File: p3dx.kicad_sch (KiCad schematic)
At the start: 57 parts, among them J10 Switched Radio, J12 IR2, J18 IR3, J19 Unlabeled, J28 H8 MICRO-CONTROLLER, J30 Charger, J31 +12V_BAT, J32 GND_BAT, J37 Cooling Fan, J38 Unlabeled, J8 IR0, J9 IR1, Q10 NPN, Q12 NPN, Q13 NPN, Q17 IRF5305, Q18 IRF5305, Q19 IRF5305, Q20 IRF5305, Q9 NPN, U10 TS922I, U11 LM35DT, U3 74HC14, U7 PT78ST105V, U8 74HC14, U9 TS922I

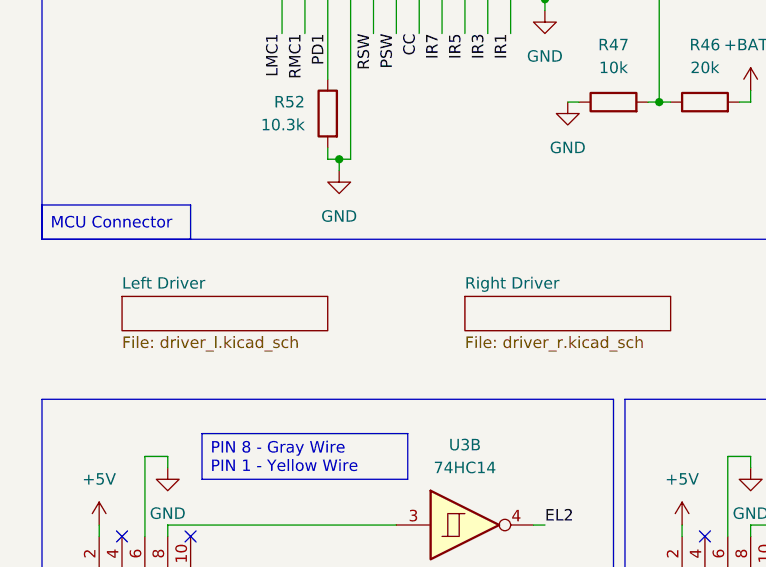
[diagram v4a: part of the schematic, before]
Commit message: Upgrad left driver scheme
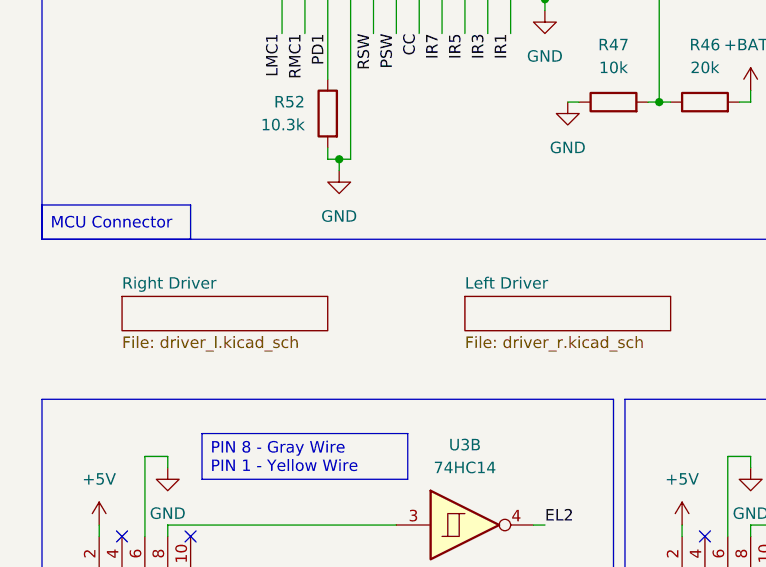
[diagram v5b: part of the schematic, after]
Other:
- sheet Left Driver: file driver_l.kicad_sch -> driver_r.kicad_sch
- sheet Right Driver: file driver_r.kicad_sch -> driver_l.kicad_sch
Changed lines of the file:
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@@
 			(color 0 0 0 0.0000)
 		)
-		(property "Sheetname" "Right Driver"
+		(property "Sheetname" "Left Driver"
 			(at 59.69 78.0284 0)
 			(effects
@@
 			(color 0 0 0 0.0000)
 		)
-		(property "Sheetname" "Left Driver"
+		(property "Sheetname" "Right Driver"
 			(at 21.59 78.0284 0)
 			(effects

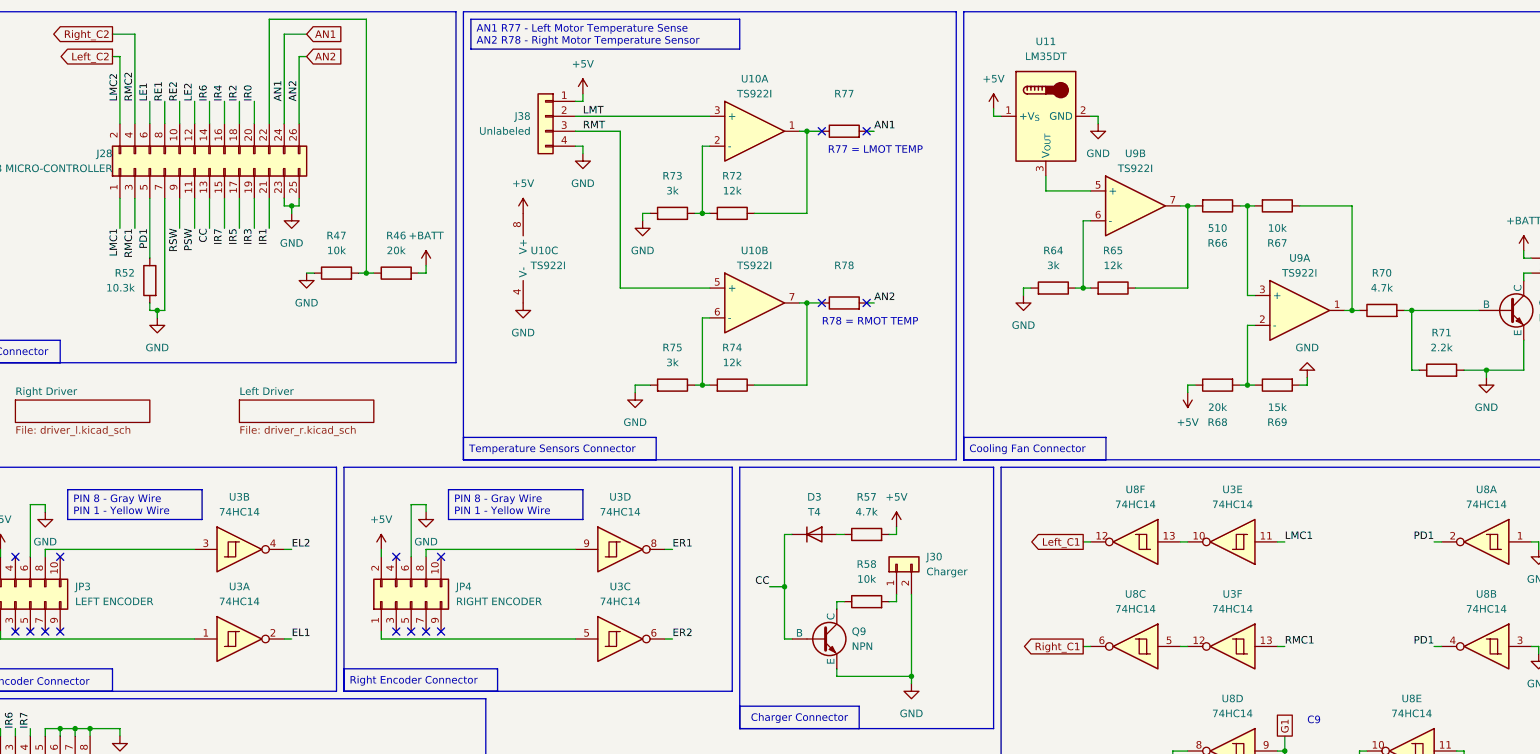
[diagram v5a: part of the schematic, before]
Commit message: Update J28 pin name
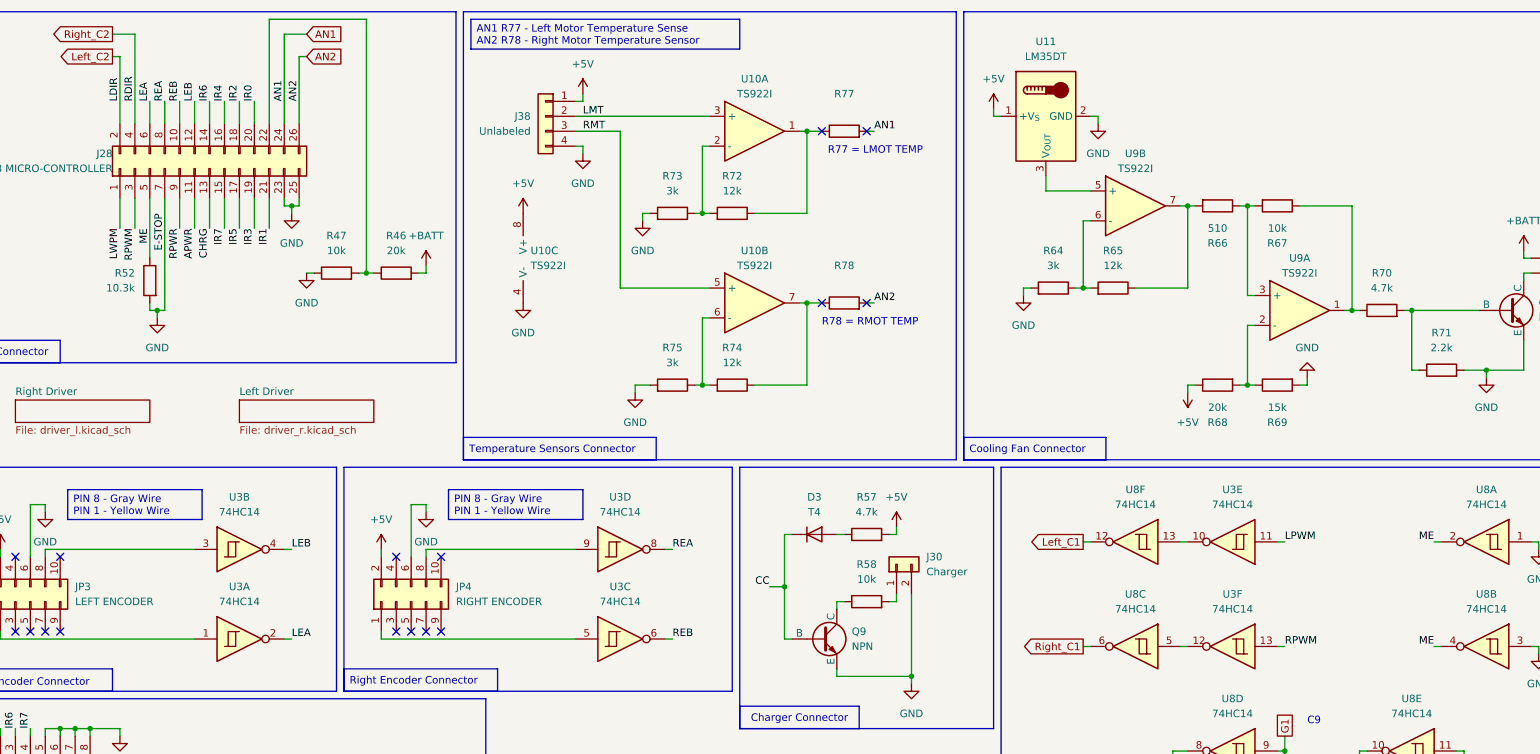
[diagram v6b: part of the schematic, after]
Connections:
- net LE1 is gone; now on net LEA: J28.6 (Pin_6)
- net LE2 is gone; now on net LEB: J28.12 (Pin_12)
- net RE1 is gone; now on net REA: J28.8 (Pin_8)
- net RE2 is gone; now on net REB: J28.10 (Pin_10)
- net CC: no longer J28.13 (Pin_13)
- net PSW: no longer J28.11 (Pin_11)
- net RSW: no longer J28.9 (Pin_9)
- net EL1 renamed LEA
- net EL2 renamed LEB
- net ER1 renamed REA
- net ER2 renamed REB
- net LMC1 renamed LPWM
- net LPWM: no longer J28.1 (Pin_1)
- net PD1 renamed ME
- net RMC1 renamed RPWM
- new net APWR: J28.11 (Pin_11)
- new net CHRG: J28.13 (Pin_13)
- new net LWPM: J28.1 (Pin_1)
- new net RPWR: J28.9 (Pin_9)
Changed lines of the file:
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@@
 		)
 	)
-	(label "LMC1"
+	(label "LPWM"
 		(at 237.49 102.87 0)
 		(effects
@@
 		)
 	)
-	(label "EL1"
+	(label "LEA"
 		(at 68.58 119.38 0)
 		(effects
@@
 		)
 	)
-	(label "LE2"
+	(label "LEB"
 		(at 52.07 27.94 90)
 		(effects
@@
 		)
 	)
-	(label "PD1"
+	(label "ME"
 		(at 262.89 102.87 180)
 		(effects
@@
 		)
 	)
-	(label "RMC1"
+	(label "RPWM"
 		(at 237.49 120.65 0)
 		(effects
@@
 		)
 	)
-	(label "RE2"
+	(label "REB"
 		(at 49.53 27.94 90)
 		(effects
@@
 		)
 	)
-	(label "RMC2"
+	(label "RDIR"
 		(at 41.91 27.94 90)
 		(effects
@@
 		)
 	)
-	(label "CC"
+	(label "CHRG"
 		(at 54.61 49.53 270)
 		(effects
@@
 		)
 	)
-	(label "PD1"
+	(label "ME"
 		(at 262.89 120.65 180)
 		(effects
@@
 		)
 	)
-	(label "RMC1"
+	(label "RPWM"
 		(at 41.91 49.53 270)
 		(effects
@@
 		)
 	)
-	(label "LMC2"
+	(label "LDIR"
 		(at 39.37 27.94 90)
 		(effects
@@
 		)
 	)
-	(label "RE1"
+	(label "REA"
 		(at 46.99 27.94 90)
 		(effects
@@
 		)
 	)
+	(label "E-STOP"
+		(at 46.99 46.99 270)
+		(effects
+			(font
+				(size 1.27 1.27)
+			)
+			(justify right bottom)
+		)
+	)
 	(label "IR2"
 		(at 80.01 147.32 270)
@@
 		)
 	)
-	(label "RSW"
+	(label "RPWR"
 		(at 49.53 49.53 270)
 		(effects
@@
 		)
 	)
-	(label "LMC1"
+	(label "LWPM"
 		(at 39.37 49.53 270)
 		(effects
@@
 		)
 	)
-	(label "PSW"
+	(label "APWR"
 		(at 52.07 49.53 270)
 		(effects
@@
 		)
 	)
-	(label "ER1"
+	(label "REA"
 		(at 133.35 104.14 0)
 		(effects
@@
 		)
 	)
-	(label "PD1"
+	(label "ME"
 		(at 44.45 49.53 270)
 		(effects
@@
 		)
 	)
-	(label "LE1"
+	(label "LEA"
 		(at 44.45 27.94 90)
 		(effects
@@
 		)
 	)
-	(label "ER2"
+	(label "REB"
 		(at 133.35 119.38 0)
 		(effects
@@
 		)
 	)
-	(label "EL2"
+	(label "LEB"
 		(at 68.58 104.14 0)
 		(effects

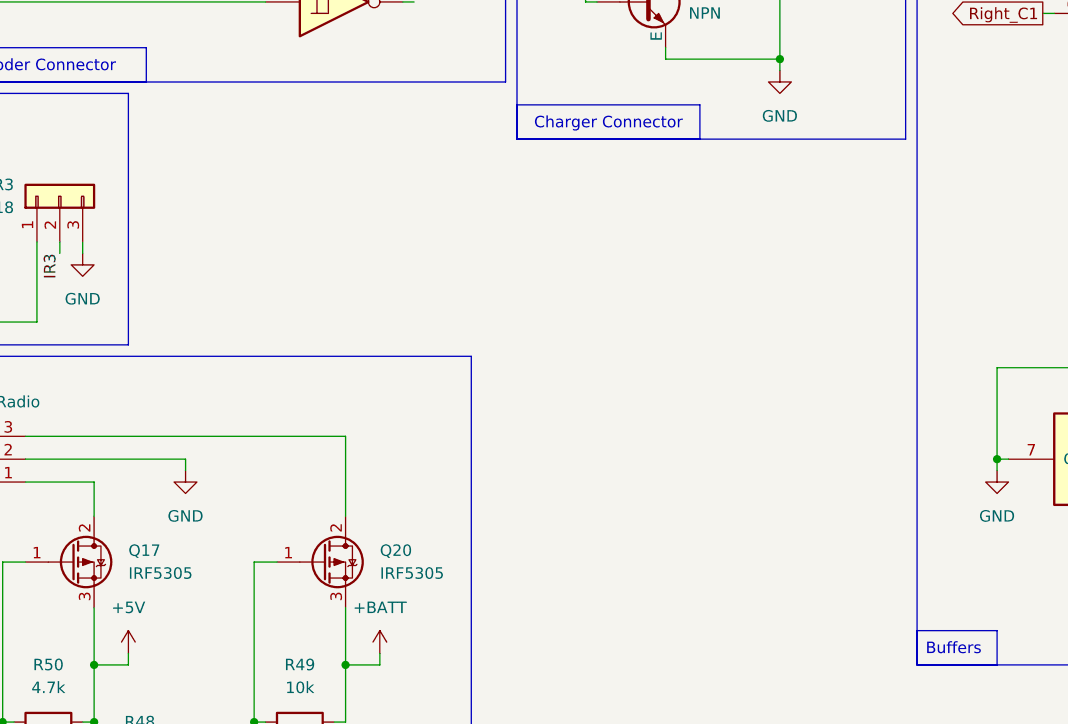
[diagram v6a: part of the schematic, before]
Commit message: Update driver scheme and added User Control Panel scheme
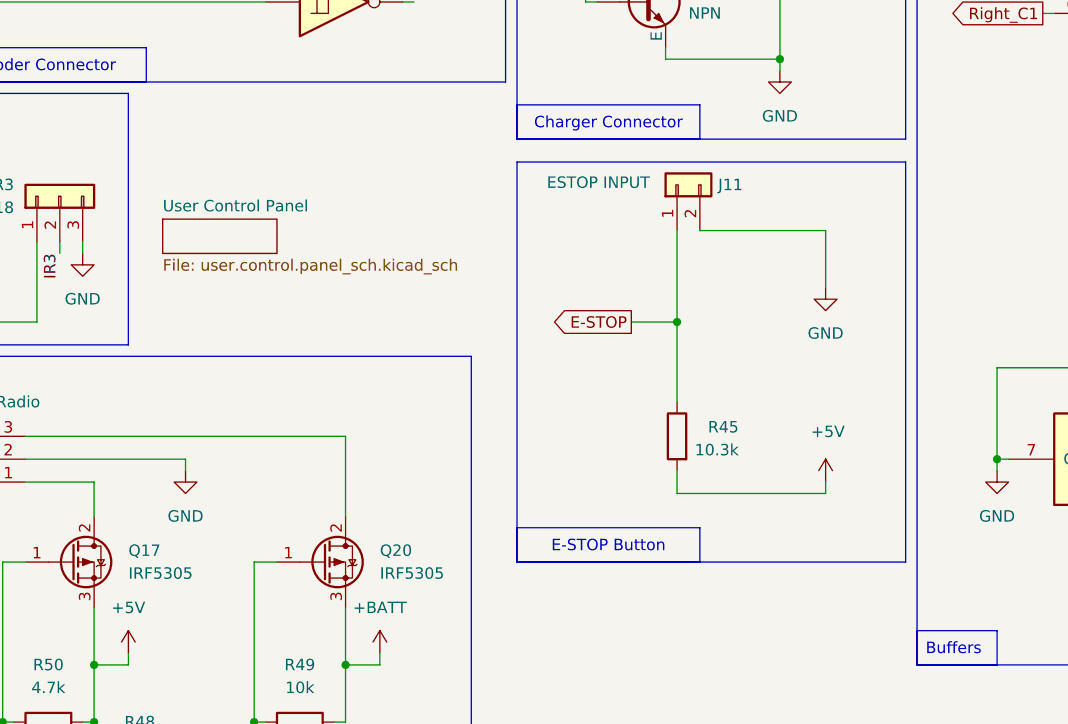
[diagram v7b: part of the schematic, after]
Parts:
- added J11: ESTOP INPUT, symbol Connector_Generic:Conn_01x02
- added R45: 10.3k, symbol Device:R
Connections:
- net +5V: now also R45.2
- net GND: now also J11.1 (Pin_1), J11.2 (Pin_2), R45.1
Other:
- added sheet User Control Panel (user.control.panel_sch.kicad_sch)
